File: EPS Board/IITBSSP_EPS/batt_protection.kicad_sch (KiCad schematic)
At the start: 11 parts, among them U1 BQ29209DRBR

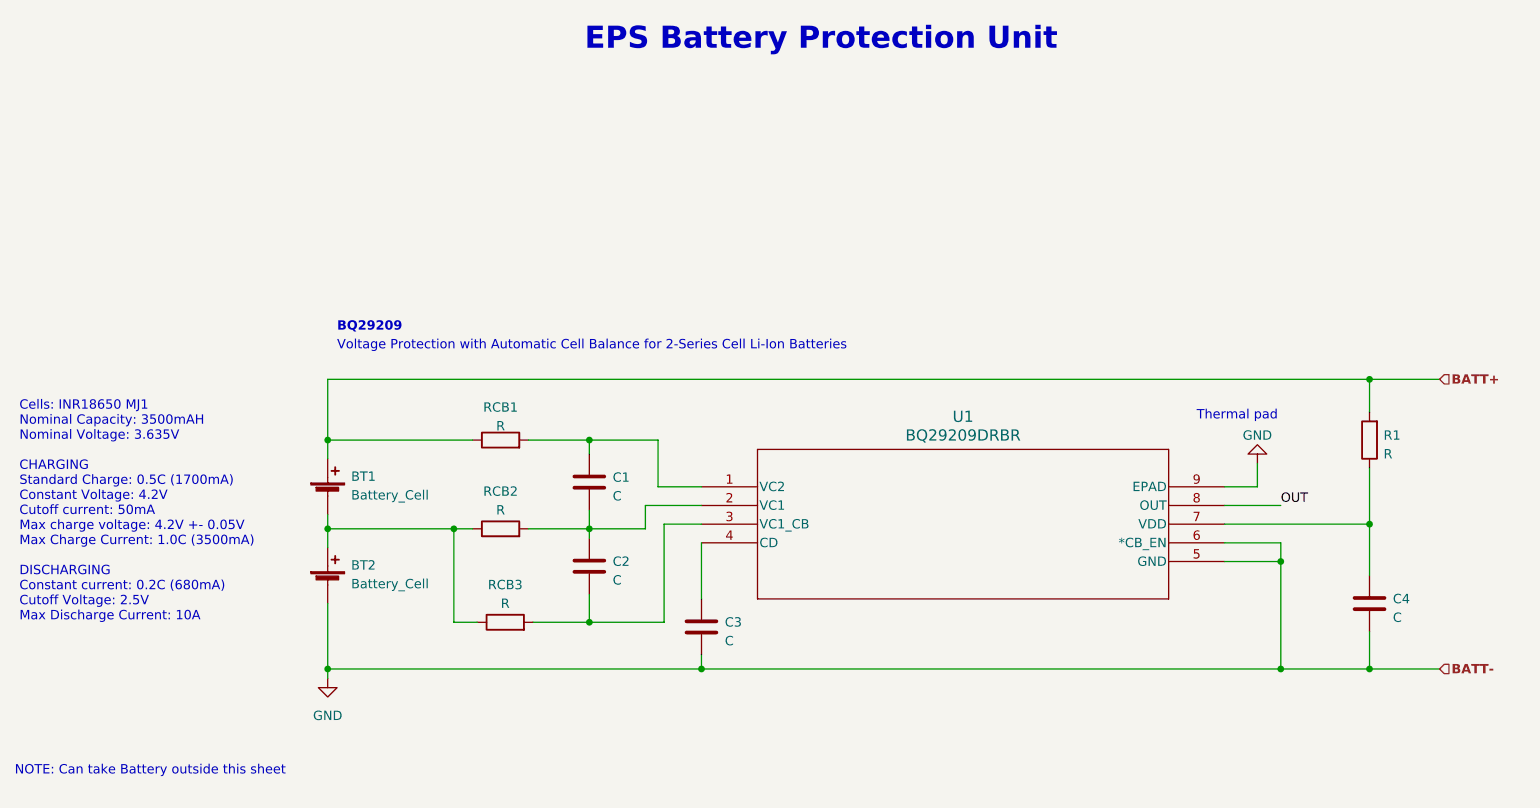
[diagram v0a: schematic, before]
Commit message: EPS Final Board
Started EPS final board schematic
yet to add dependencies of external libraries to a common folder on GitHub
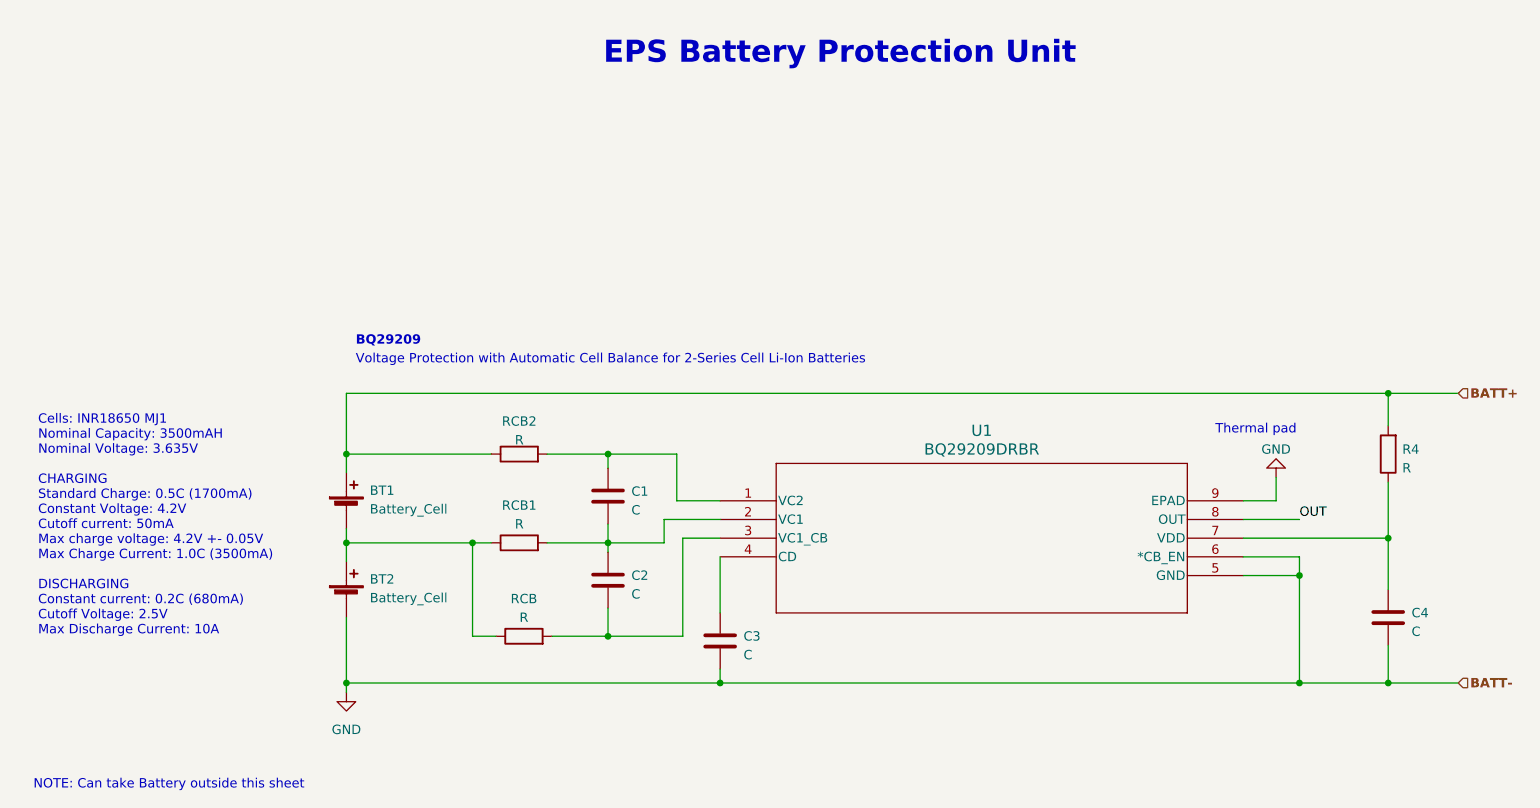
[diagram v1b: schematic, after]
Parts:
- removed R1, RCB3: R, symbol Device:R
- added R4, RCB: R, symbol Device:R
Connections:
- net BATT+: now also RCB2.1, R4.2; no longer RCB1.1
- net at C1.1, U1.1 (VC2): now also RCB2.2; no longer RCB1.2
- net at C1.2, C2.1, U1.2 (VC1): now also RCB1.2; no longer RCB2.2
- net at C4.1, U1.7 (VDD): now also R4.1
- net at BT1.2 (-), BT2.1 (+): now also RCB1.1, RCB.1; no longer RCB2.1
- net at C2.2, U1.3 (VC1_CB): now also RCB.2
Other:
- company: IIT Bombay Student Satellite Program -> (none)
- title: Battery Protection Unit -> (none)
